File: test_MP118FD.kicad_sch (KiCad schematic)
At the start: 2 parts

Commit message: condensadores
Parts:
- added C2, C3: 680uF, Capacitor_THT:CP_Radial_D30.0mm_P10.00mm_SnapIn, symbol Device:C_Polarized
- added C4, C5, C6: 1uF, Capacitor_SMD:C_2220_5750Metric, symbol Device:C
- C1: value C -> 1uF; footprint (none) -> Capacitor_SMD:C_2220_5750Metric; Fabricante (none) -> RS: 146-4260; Precio (none) -> 5,81 €. 2 unidades

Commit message: con componentes
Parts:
- added C7: 10 pF, Capacitor_THT:C_Disc_D7.5mm_W5.0mm_P7.50mm, symbol Device:C
- added PB1: SD, Button_Switch_THT:SW_PUSH-12mm, symbol Switch:SW_MEC_5E
- added PB2: RESET, Button_Switch_THT:SW_PUSH-12mm, symbol Switch:SW_MEC_5E
- added R1: R_Shunt, Library:Shunt PBV Isabellenhutte 17,78x7,62, symbol Device:R_Shunt
- added R2: 1K, Resistor_THT:R_Axial_DIN0207_L6.3mm_D2.5mm_P7.62mm_Horizontal, symbol Device:R
- added R3, R4: 10K, Resistor_THT:R_Axial_DIN0207_L6.3mm_D2.5mm_P7.62mm_Horizontal, symbol Device:R
- added R5: 10, symbol Device:Heater
- added RLIM1, RLIM2: 1, Resistor_THT:R_Radial_Power_L16.1mm_W9.0mm_P7.37mm, symbol Device:R

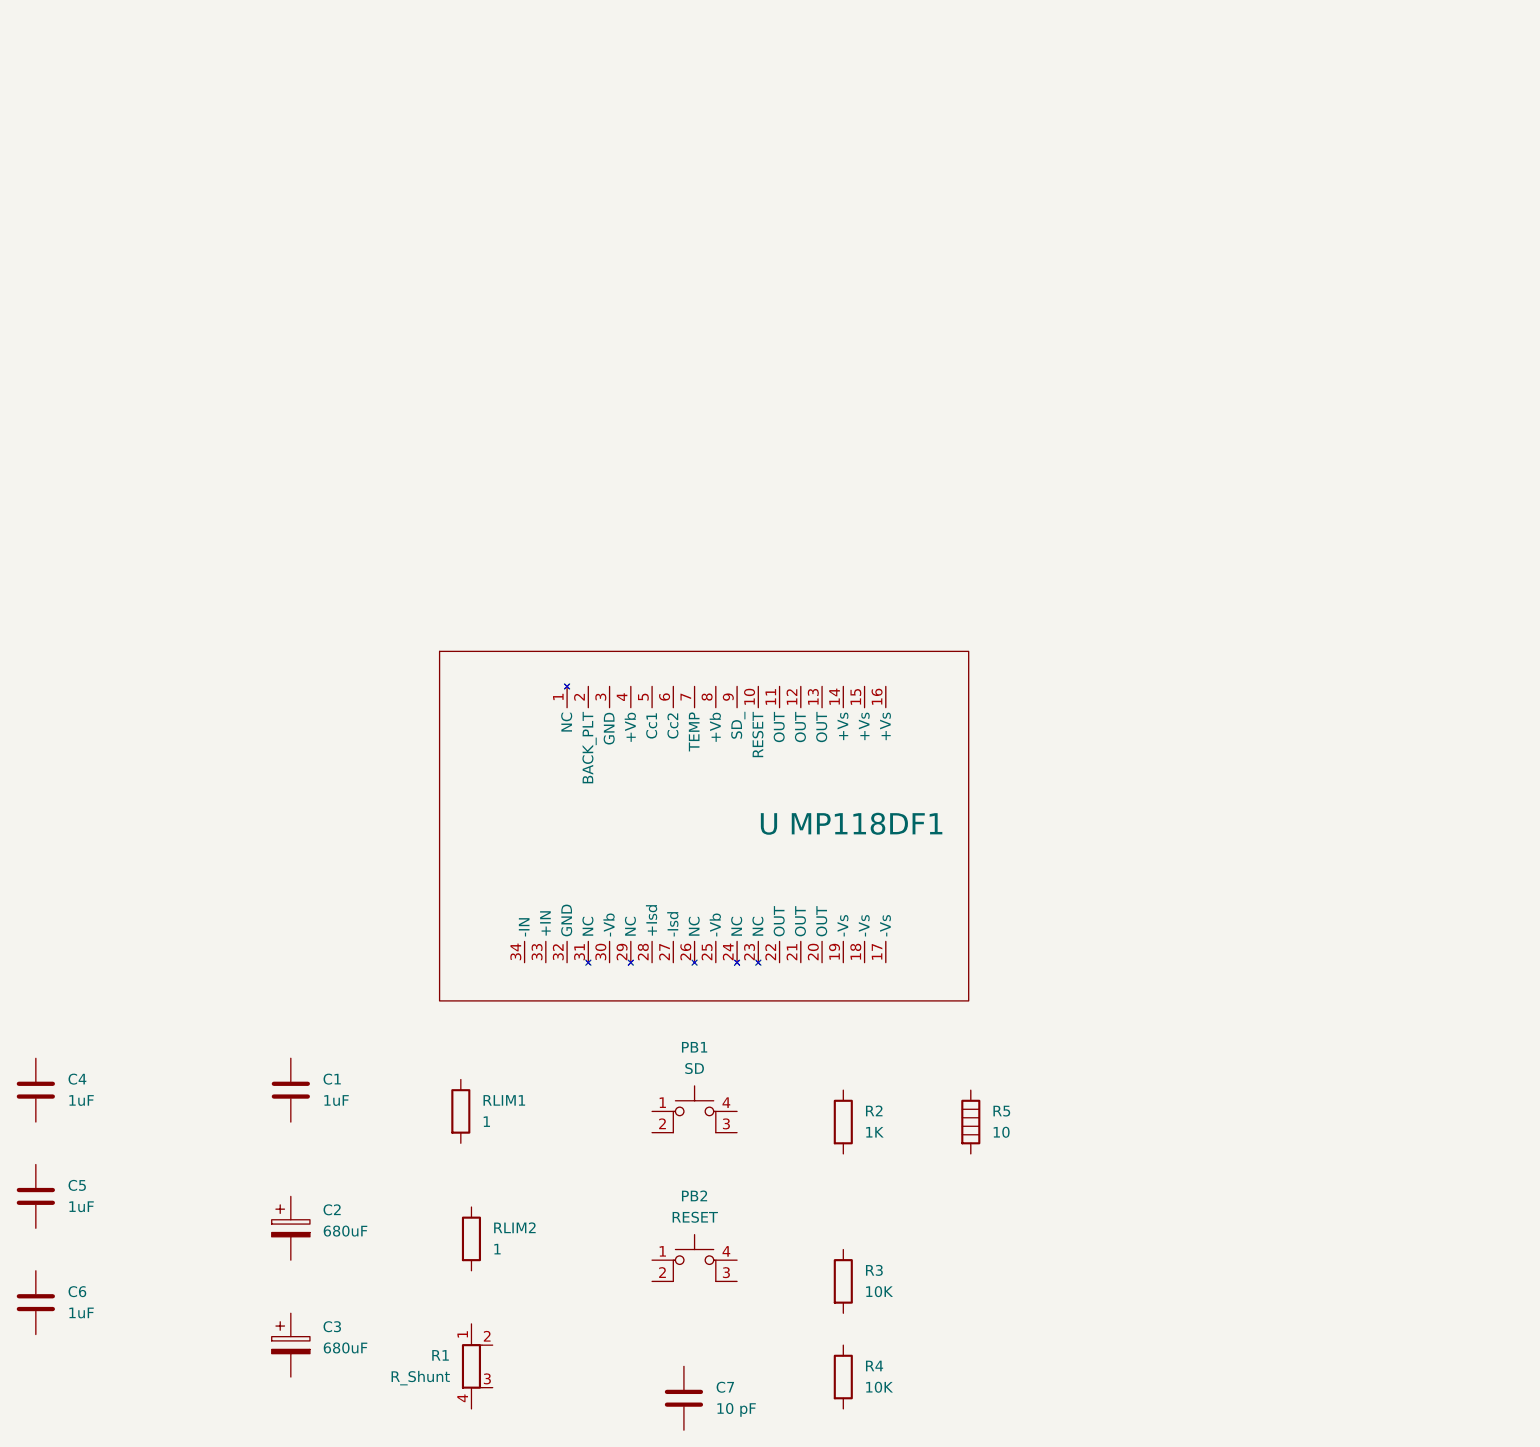
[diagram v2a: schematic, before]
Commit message: Primer esquema, sin resistencias en serie, sin carga
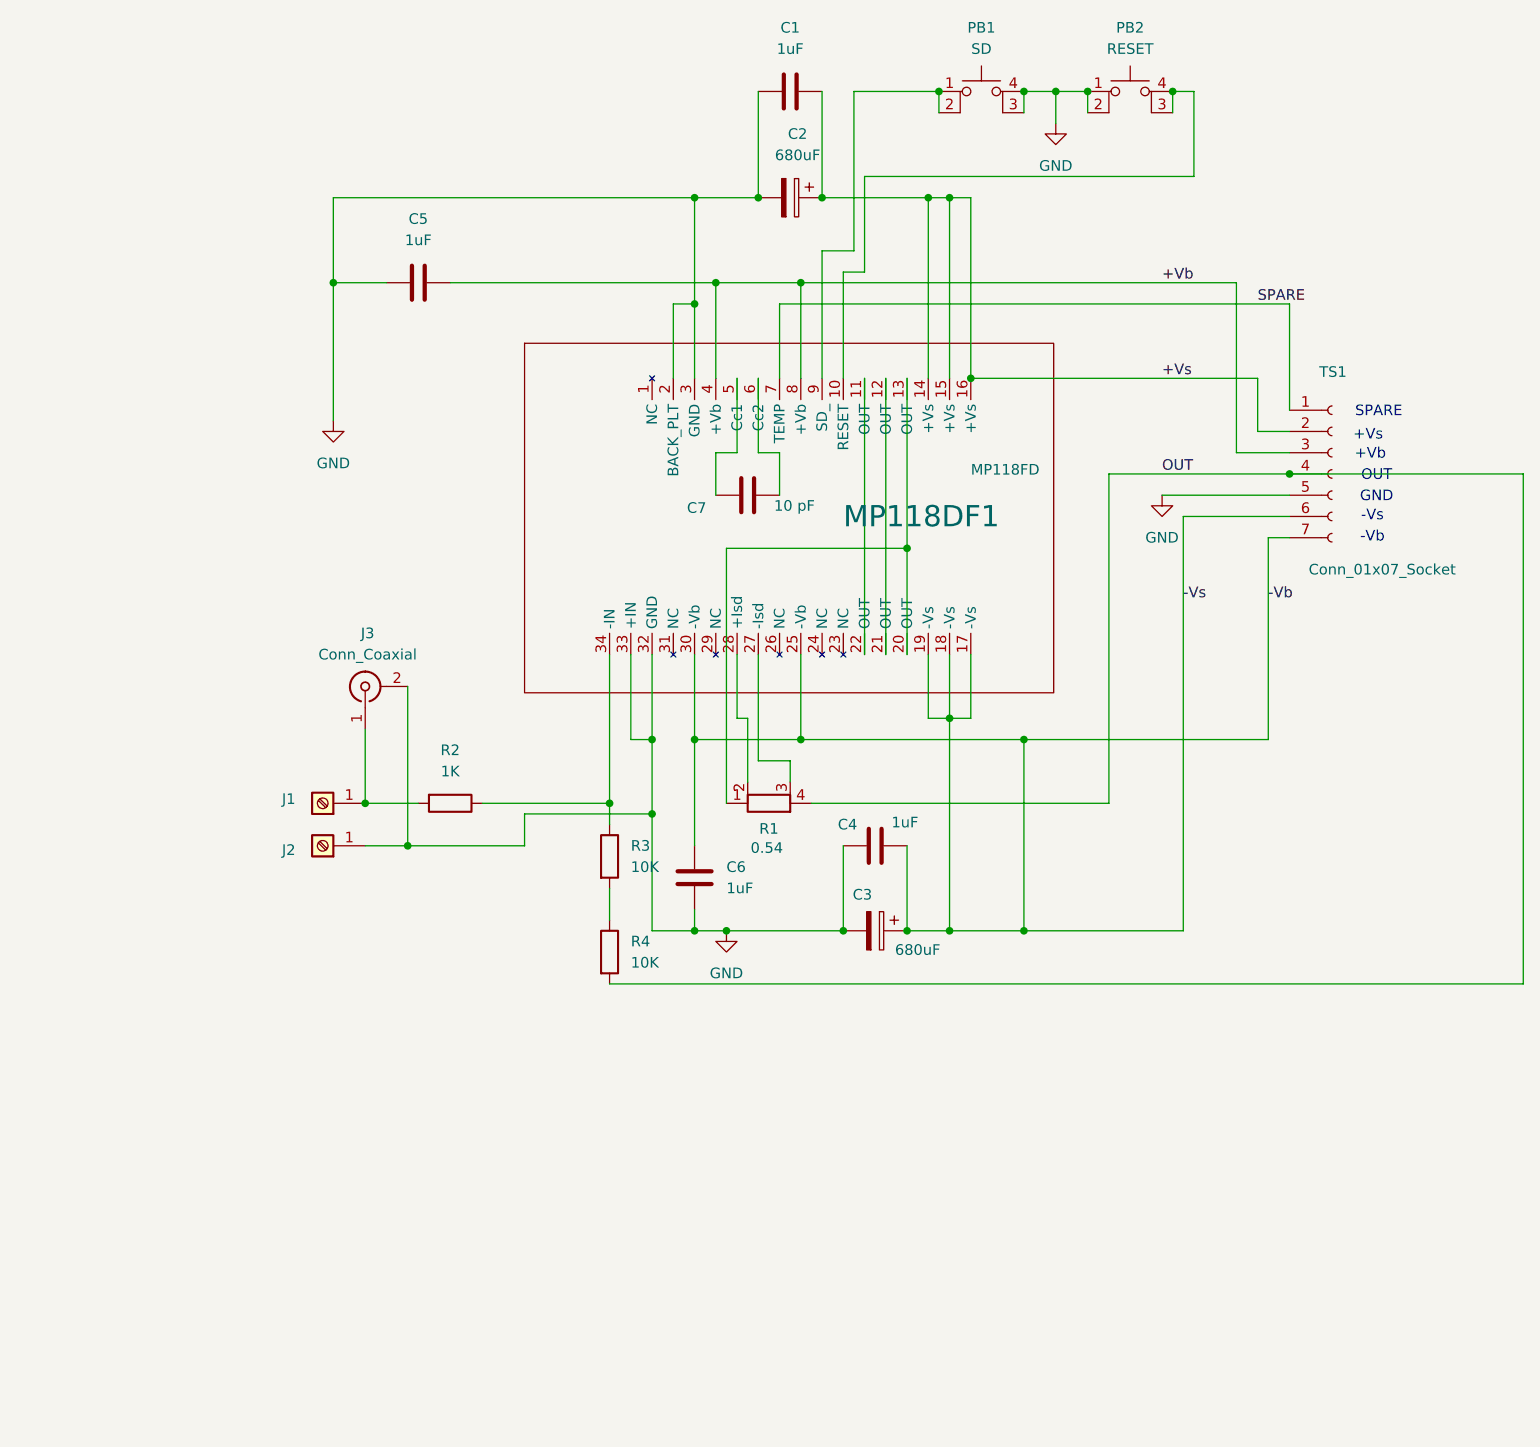
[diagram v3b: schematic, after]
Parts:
- removed R5: 10, symbol Device:Heater
- removed RLIM1, RLIM2: 1, Resistor_THT:R_Radial_Power_L16.1mm_W9.0mm_P7.37mm, symbol Device:R
- added J1, J2: Screw_Terminal_01x01, TerminalBlock_MetzConnect:TerminalBlock_MetzConnect_360271_1x01_Horizontal_ScrewM3.0_Boxed, symbol Connector:Screw_Terminal_01x01
- added J3: Conn_Coaxial, Connector_Coaxial:BNC_TEConnectivity_1478204_Vertical, symbol Connector:Conn_Coaxial
- added TS1: Conn_01x07_Socket, Connector_Phoenix_SPT:PhoenixContact_SPT_5_7-H-7.5-ZB_1x07_P7.5mm_Horizontal, symbol Apex:Conn_01x07_Socket
- MP118DF1: renamed from U MP118DF1; value ~ -> MP118FD; footprint (none) -> Library:MP118; Proveedor (none) -> System-70000124
- R1: value R_Shunt -> 0.54
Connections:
- net -Vb: now reaches C6.1
- net -Vb: now also C3.1, C4.1, MP118DF1.17 (-Vs), MP118DF1.18 (-Vs), MP118DF1.19 (-Vs), MP118DF1.25 (-Vb), MP118DF1.30 (-Vb), TS1.6 (Pin_6), TS1.7 (Pin_7)
- net GND: now reaches C6.2
- net GND: now also C1.2, C2.2, C3.2, C4.2, C5.1, MP118DF1.2 (BACK_PLT), MP118DF1.3 (GND), MP118DF1.32 (GND), MP118DF1.33 (+IN), PB1.3 (K), PB1.4 (A), PB2.1, PB2.2, J2.1 (Pin_1), J3.2 (Ext), TS1.5 (Pin_5)
- net at C7.1: now also MP118DF1.6 (Cc2)
- net at C7.2: now also MP118DF1.5 (Cc1)
- net at PB1.1: now also MP118DF1.9 (SD_), PB1.2
- net at R4.1: now also R3.2
- net OUT: now reaches R4.2
- net OUT: now also R1.4, TS1.4 (Pin_4)
- net at R3.1: now also MP118DF1.34 (-IN), R2.1
- net at PB2.3 (K): now also MP118DF1.10 (RESET), PB2.4 (A)
- net at R2.2: now also J1.1 (Pin_1), J3.1 (In)
- net at R1.1: now also MP118DF1.13 (OUT), MP118DF1.20 (OUT)
- net at R1.2: now also MP118DF1.28 (+Isd)
- net at R1.3: now also MP118DF1.27 (-Isd)
- net +Vs: now reaches C1.1
- net +Vs: now also C2.1, MP118DF1.14 (+Vs), MP118DF1.15 (+Vs), MP118DF1.16 (+Vs), TS1.2 (Pin_2)
- net +Vb: now reaches C5.2
- net +Vb: now also MP118DF1.4 (+Vb), MP118DF1.8 (+Vb), TS1.3 (Pin_3)
- net at MP118DF1.11 (OUT): now also MP118DF1.22 (OUT)
- net at MP118DF1.12 (OUT): now also MP118DF1.21 (OUT)
- net SPARE: now reaches MP118DF1.7 (TEMP)
- net SPARE: now also TS1.1 (Pin_1)
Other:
- note added: "+Vb"
- note added: "+Vs"
- note added: "-Vb"
- note added: "-Vs"
- note added: "GND"
- note added: "OUT"
- note added: "SPARE"
- moved on the sheet: C1, C2, C3, C4, C5, C6, C7, MP118DF1, PB1, PB2, R1, R2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

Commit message: correccion pines mp118 y stp del co0nector phoenix 7p
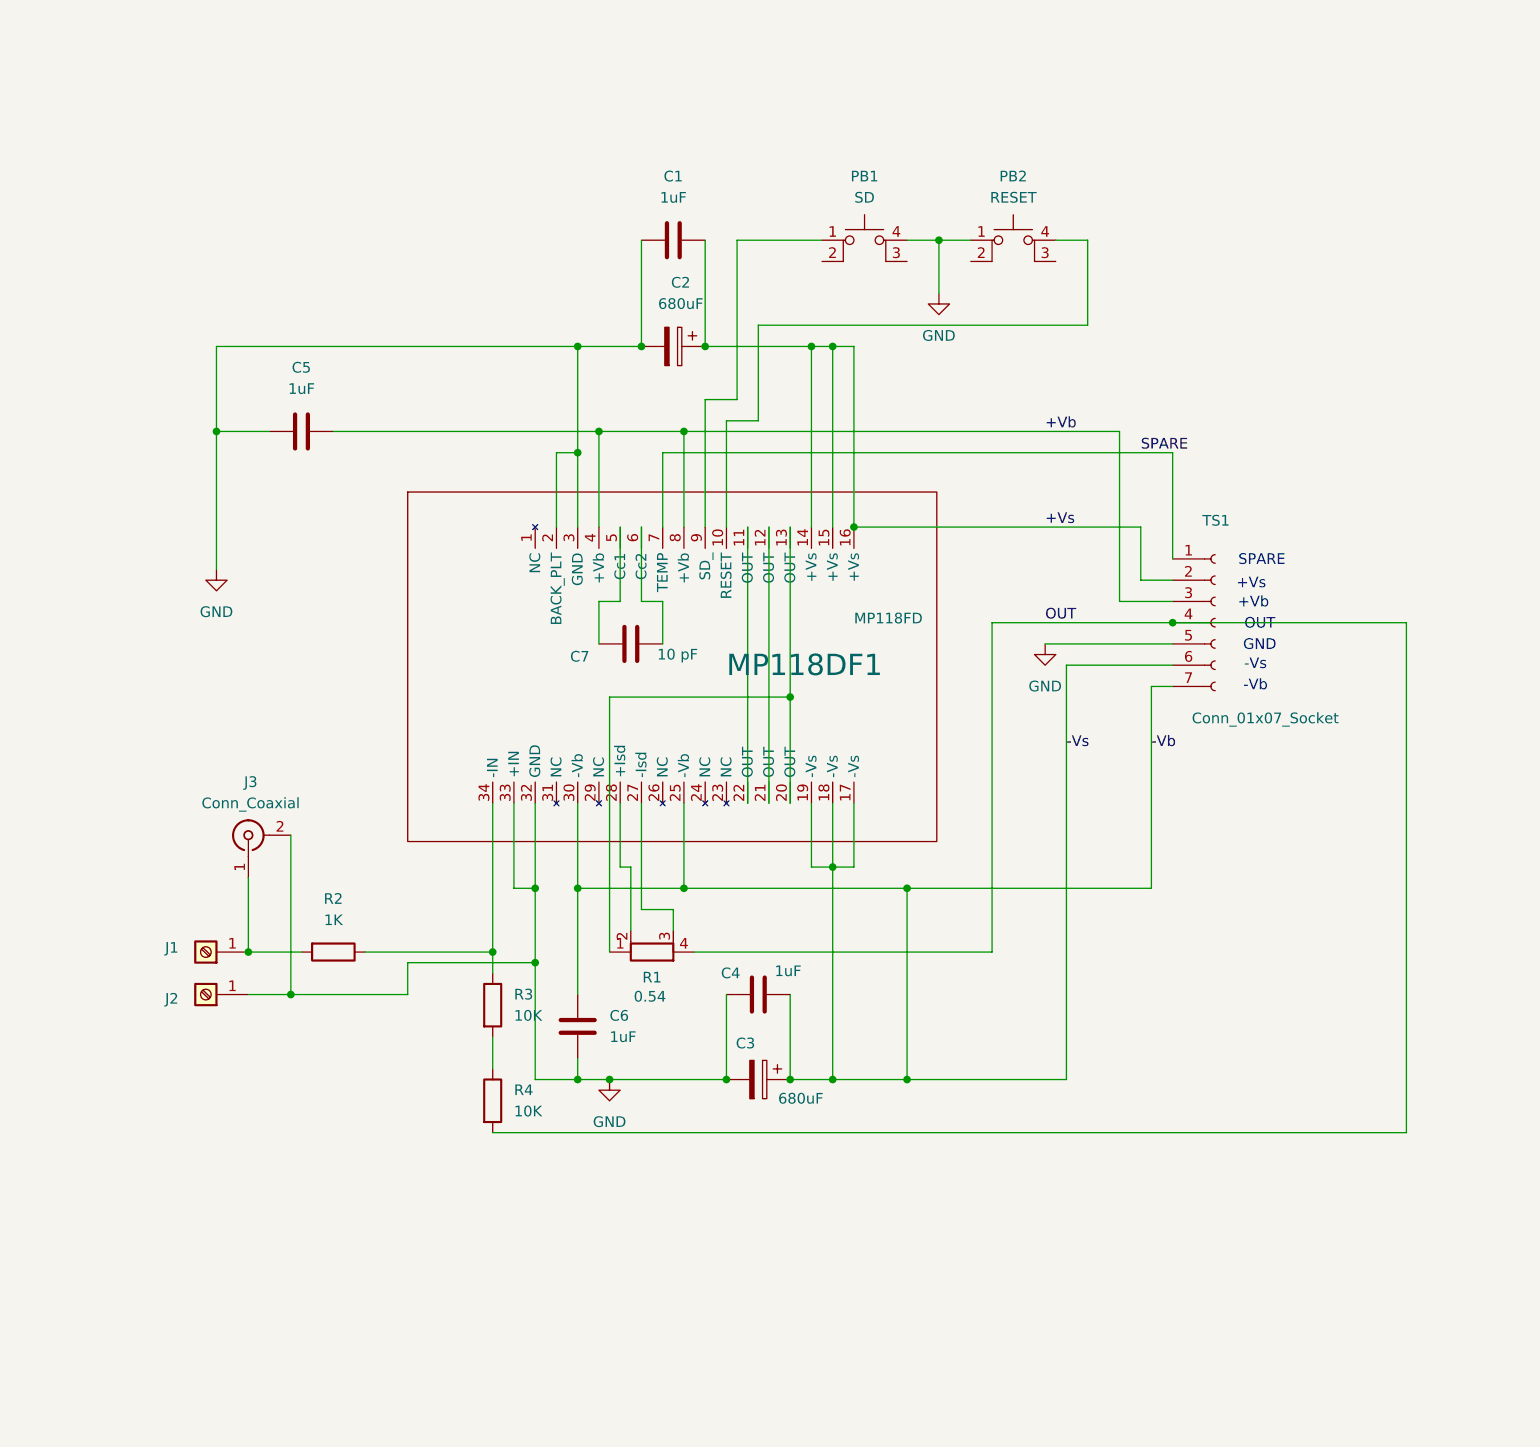
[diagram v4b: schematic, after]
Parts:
- PB1: footprint Button_Switch_THT:SW_PUSH-12mm -> Library:SW_PUSH-12mm; Proveedor RS: 443-676 -> RS: 443-676 RS: 378-6763
- PB2: footprint Button_Switch_THT:SW_PUSH-12mm -> Library:SW_PUSH-12mm
- TS1: footprint Connector_Phoenix_SPT:PhoenixContact_SPT_5_7-H-7.5-ZB_1x07_P7.5mm_Horizontal -> Library:PhoenixContact_SPT_5_7-H-7.5-ZB_1x07_P7.5mm_Horizontal
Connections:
- net GND: no longer PB1.3 (K), PB2.2
- net at MP118DF1.9 (SD_), PB1.1: no longer PB1.2
- net at MP118DF1.10 (RESET), PB2.4 (A): no longer PB2.3 (K)
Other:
- moved on the sheet: C1, C2, C3, C4, C5, C6, C7, J1, J2, J3, MP118DF1, PB1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
